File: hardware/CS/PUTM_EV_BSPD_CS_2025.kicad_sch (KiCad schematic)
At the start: 25 parts, among them J1 To BSPD, J2 LEM, U1 MC78M12CDTG, U2 LM1117IMP-5.0, U3 Opamp_Quad

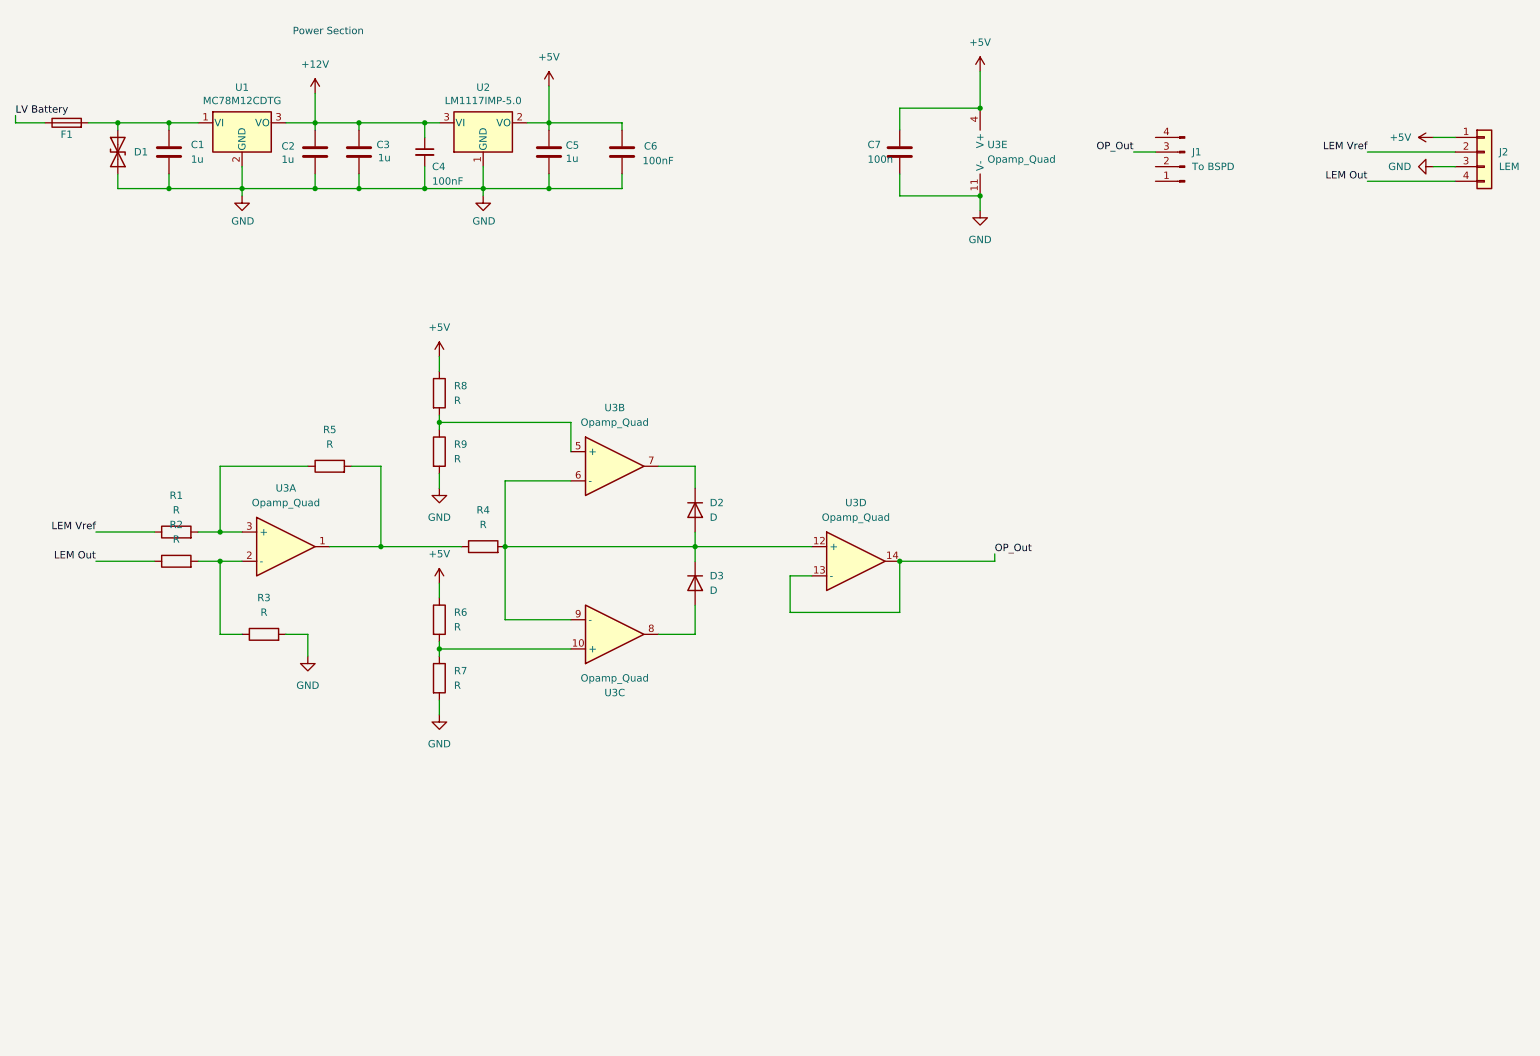
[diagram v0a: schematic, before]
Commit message: Timing Changed + Documented
Changed 10 second autoreset timer to a 555 in one-shot configuration. Also documented BSPD Board.
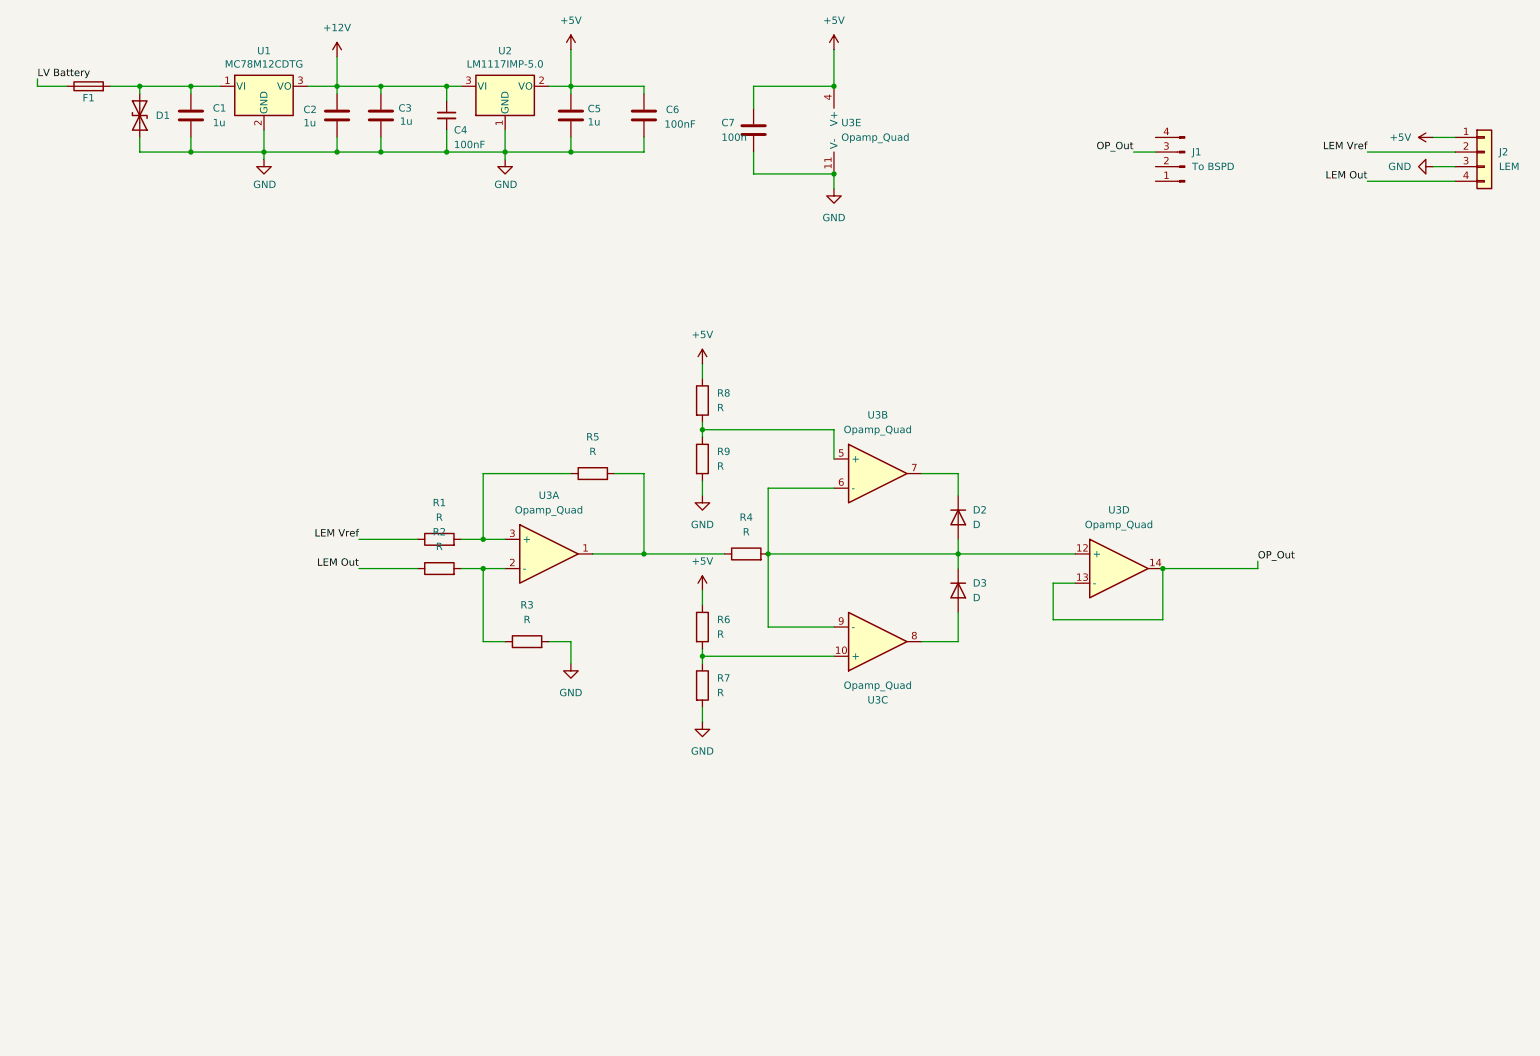
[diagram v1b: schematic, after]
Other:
- note removed: "Power Section"
- moved on the sheet: C1, C2, C3, C4, C5, C6, C7, D1, D2, D3, F1, R1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

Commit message: Minor documentation + schematic changes
Changed documentation to more descriptive, fixed zajebas where OpAmps were placed instead of comparators. 
Changed resistors values on CS board
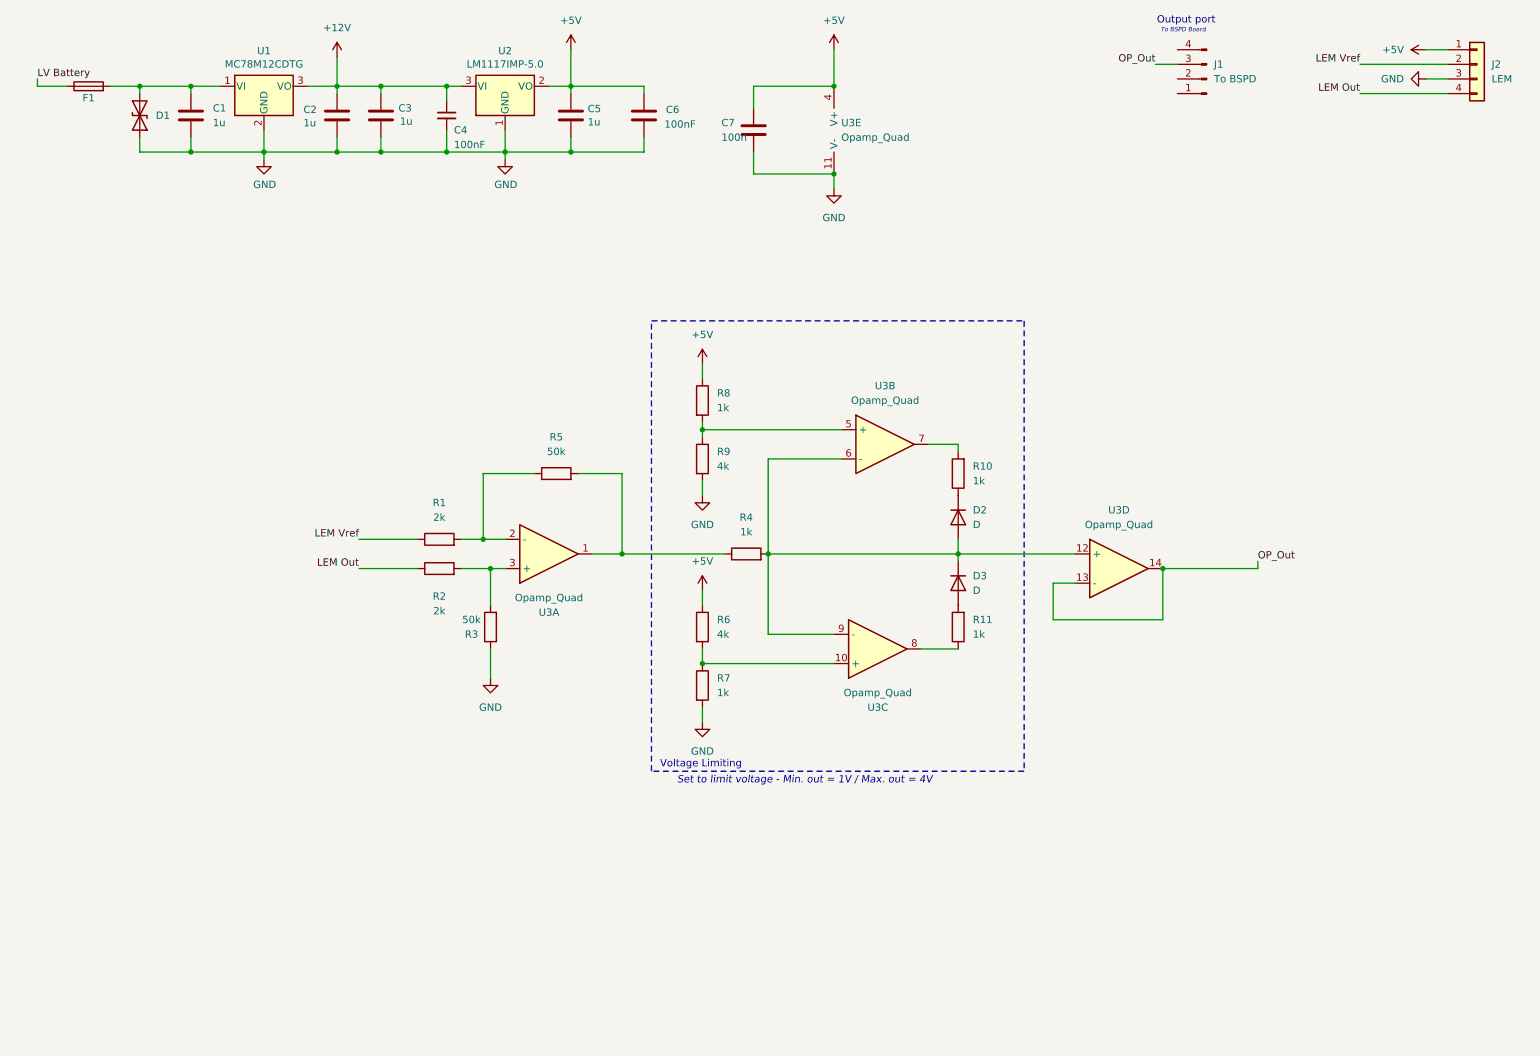
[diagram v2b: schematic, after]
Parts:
- added R10, R11: 1k, symbol Device:R
- R1, R2: value R -> 2k
- R3, R5: value R -> 50k
- R4, R7, R8: value R -> 1k
- R6, R9: value R -> 4k
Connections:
- net GND: now also R3.1; no longer R3.2
- net at R1.2, R5.1: now also U3.2 (-); no longer U3.3 (+)
- net at D3.2 (A): now also R11.2; no longer U3.8
- net at D2.1 (K): now also R10.1; no longer U3.7
- new net: R10.2, U3.7
- new net: R2.2, R3.2, U3.3 (+)
- new net: R11.1, U3.8
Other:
- note added: "Output port"
- note added: "Set to limit voltage - Min. out = 1V / Max. out = 4V"
- note added: "To BSPD Board"
- note added: "Voltage Limiting"
- moved on the sheet: D3, J1, J2, R3, R5, U3B, U3C

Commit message: Fixed logic errors + assigned element values
Fixed wrong logic on Brake Sensor comparators, assigned IC's and connectors, added TVS diodes on connectors.
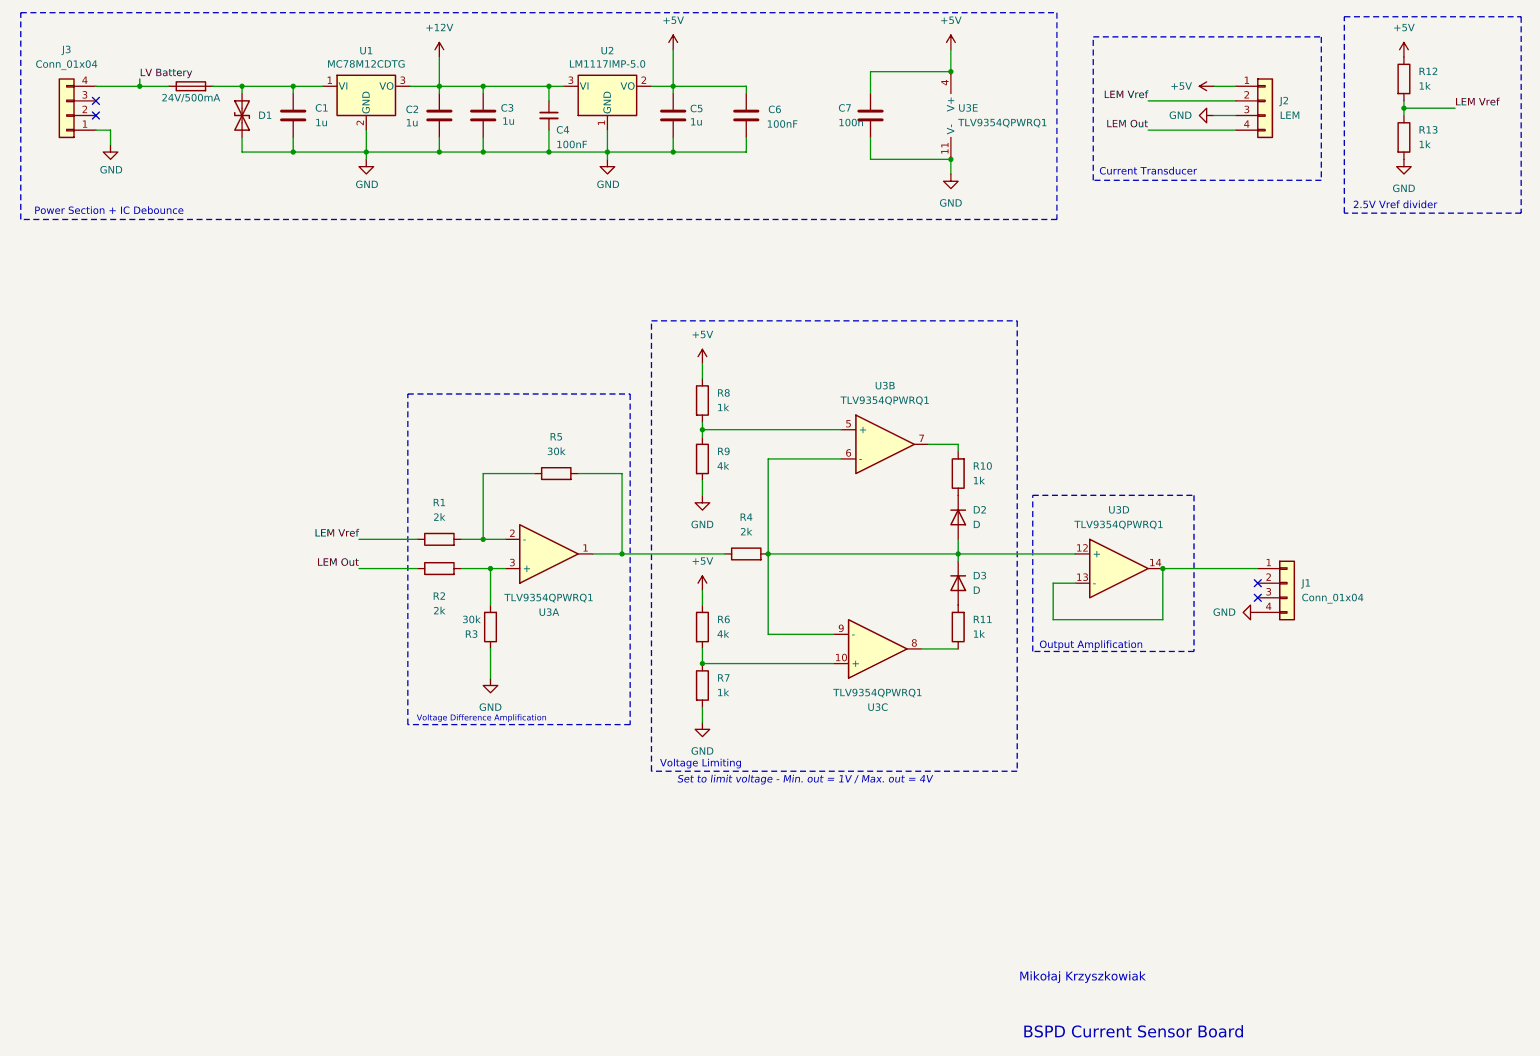
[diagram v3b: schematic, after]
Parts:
- removed J1: To BSPD, symbol Connector:Conn_01x04_Pin
- added J1, J3: Conn_01x04, symbol Connector_Generic:Conn_01x04
- added R12, R13: 1k, symbol Device:R
- D1: value 1N630xCA -> LBD52A24L01
- R3, R5: value 50k -> 30k
- R4: value 1k -> 2k
- U3: value Opamp_Quad -> TLV9354QPWRQ1
- renumbered F1 to 24V/500mA
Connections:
- net +5V: now also R12.1
- net GND: now also J1.4 (Pin_4), J3.1 (Pin_1), R13.2
- net LEM Vref: now also R12.2, R13.1
- net LV Battery : now also J3.4 (Pin_4)
- net OP_Out: no longer names the net of U3.13 (-), U3.14
- net OP_Out: now also J1.1 (Pin_1)
- no-connect marks 0 -> 4
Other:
- note added: "2.5V Vref divider"
- note added: "BSPD Current Sensor Board"
- note added: "Current Transducer"
- note added: "Mikołaj Krzyszkowiak"
- note added: "Output Amplification"
- note added: "Power Section + IC Debounce"
- note added: "Voltage Difference Amplification"
- note removed: "Output port"
- note removed: "To BSPD Board"
- moved on the sheet: 24V/500mA, C1, C2, C3, C4, C5, C6, C7, D1, J2, U1, U2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
